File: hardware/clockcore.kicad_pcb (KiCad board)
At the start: 2 copper layers, 75 x 40 mm, 60 parts, among them J1 Header, J2 Ext, J3 JTAG, J7 GCT_USB4108-GF-A, Q1 MBT3904DW1T1G, SW1 Reset, SW2 Boot, U1 AP2114H-3_3TRG1, U2 ‎SN74HCT245PWR‎, U3 ESP32-WROOM-32, U4 DS1338Z-33+, U5 FT231XS, U6 USBLC6-4SC6, Y1 32.768Hz, 12.5pF, 45kΩ

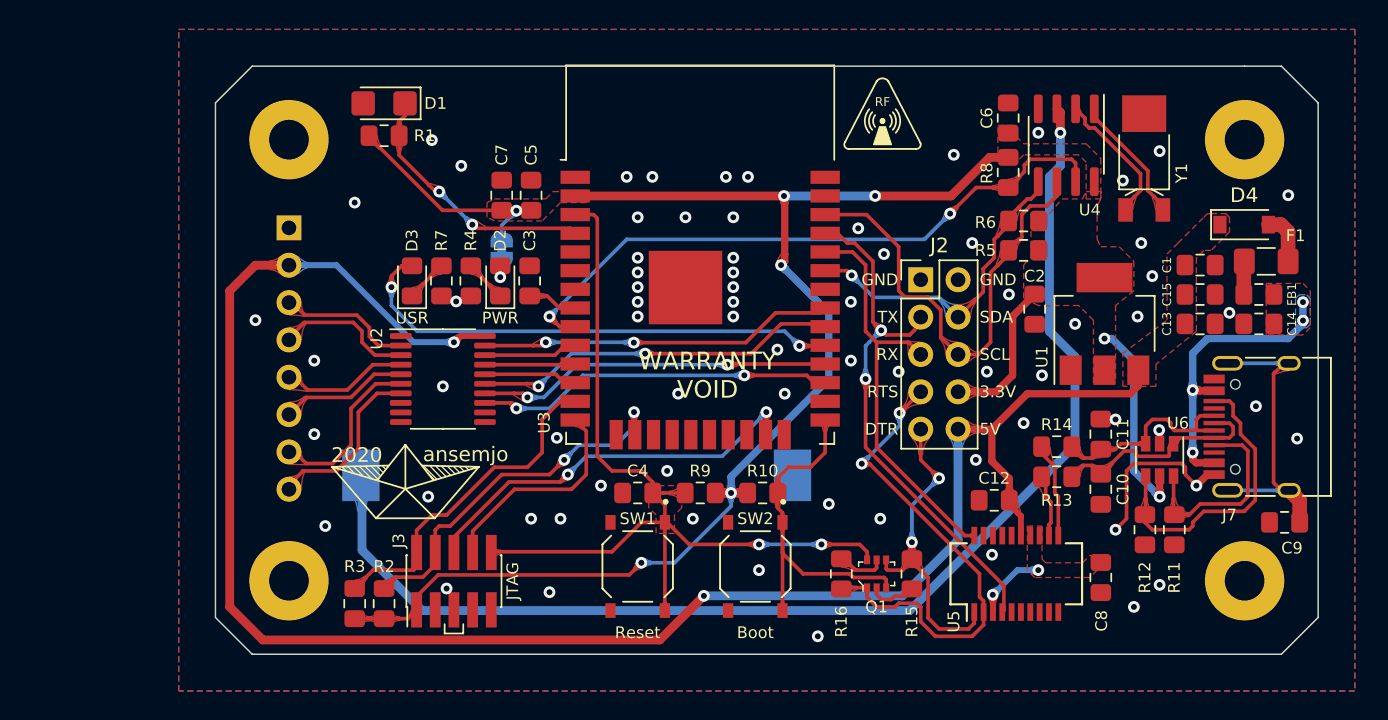
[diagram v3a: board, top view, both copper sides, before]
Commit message: add ds18b20 to clock core and reroute a few traces
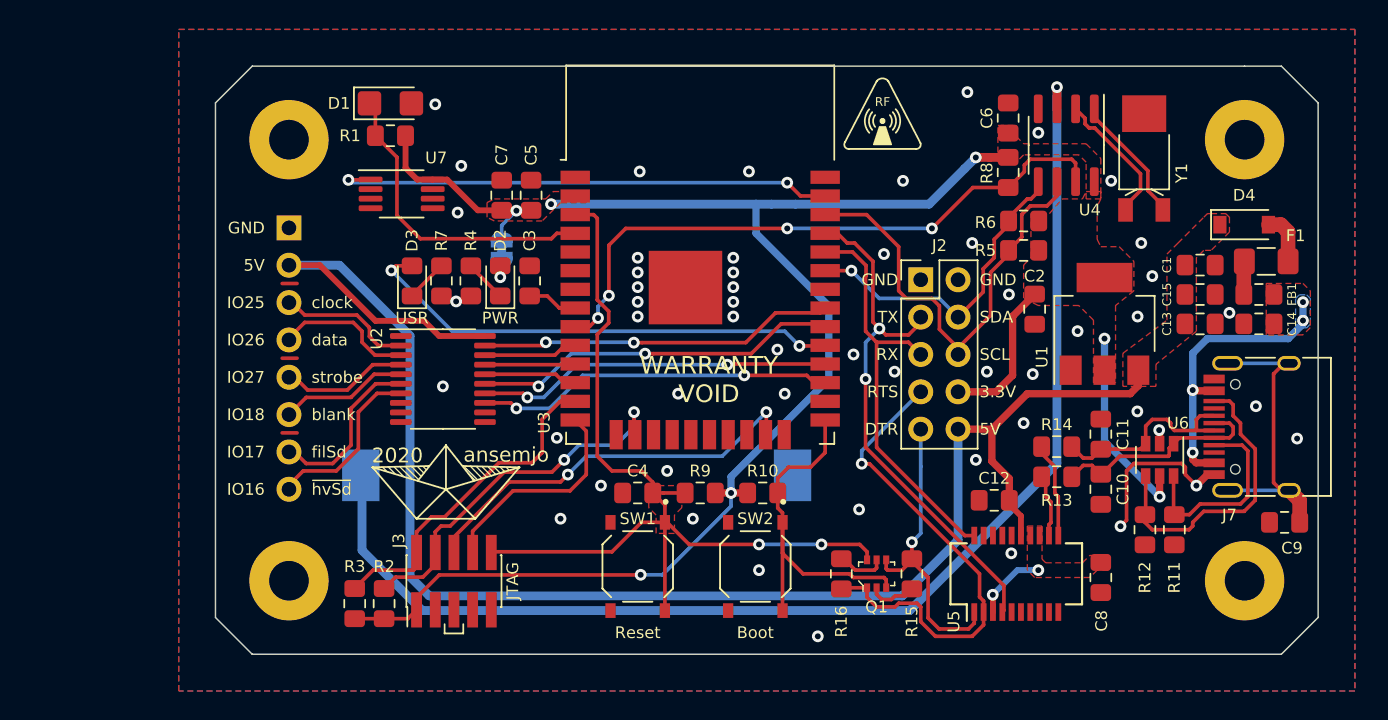
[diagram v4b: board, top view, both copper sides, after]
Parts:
- added U7: DS18B20U, Package_SO:MSOP-8_3x3mm_P0.65mm, F.Cu at (97.7, 56.2)
- moved A1 2.76 mm to (100.7, 76.3)
- moved D1 0.43 mm to (96.9, 50.0), turned to 0 degrees
- moved R1 0.43 mm to (96.9, 52.2), turned to 180 degrees
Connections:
- U3 pad 37: (no net) -> TEMP
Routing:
- net TEMP: track 0.00 -> 34.4 mm, vias 0 -> 2
- net +5V: track 125.4 -> 111.5 mm, vias 2 -> 0
- net LIGHT: track 17.9 -> 21.3 mm, vias 2 -> 0
- net GND: track 12.6 -> 15.3 mm, vias 72 -> 53
- net Net-(BT1-Pad1): track 83.9 -> 85.2 mm
- net IO_LED: track 34.9 -> 33.8 mm
- net SCL: track 31.8 -> 30.7 mm
- net DTR: track 21.8 -> 20.8 mm, vias 2 -> 1
- net RTC_SQW: track 43.9 -> 42.9 mm, vias 2 -> 4
- net CHIP_EN: track 61.3 -> 62.0 mm
- net +3V3: track 126.5 -> 126.8 mm, vias 8 -> 7
- net RTS: vias 2 -> 1
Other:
- board text added: "IO16"
- board text added: "IO17"
- board text added: "IO18"
- board text added: "IO25"
- board text added: "IO26"
- board text added: "IO27"
- board text added: "blank"
- board text added: "clock"
- board text added: "data"
- board text added: "filSd"
- board text added: "strobe"
- board text added: "~hvSd~"

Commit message: updated crystal in schematic so pin3 is gnd, added teardrops
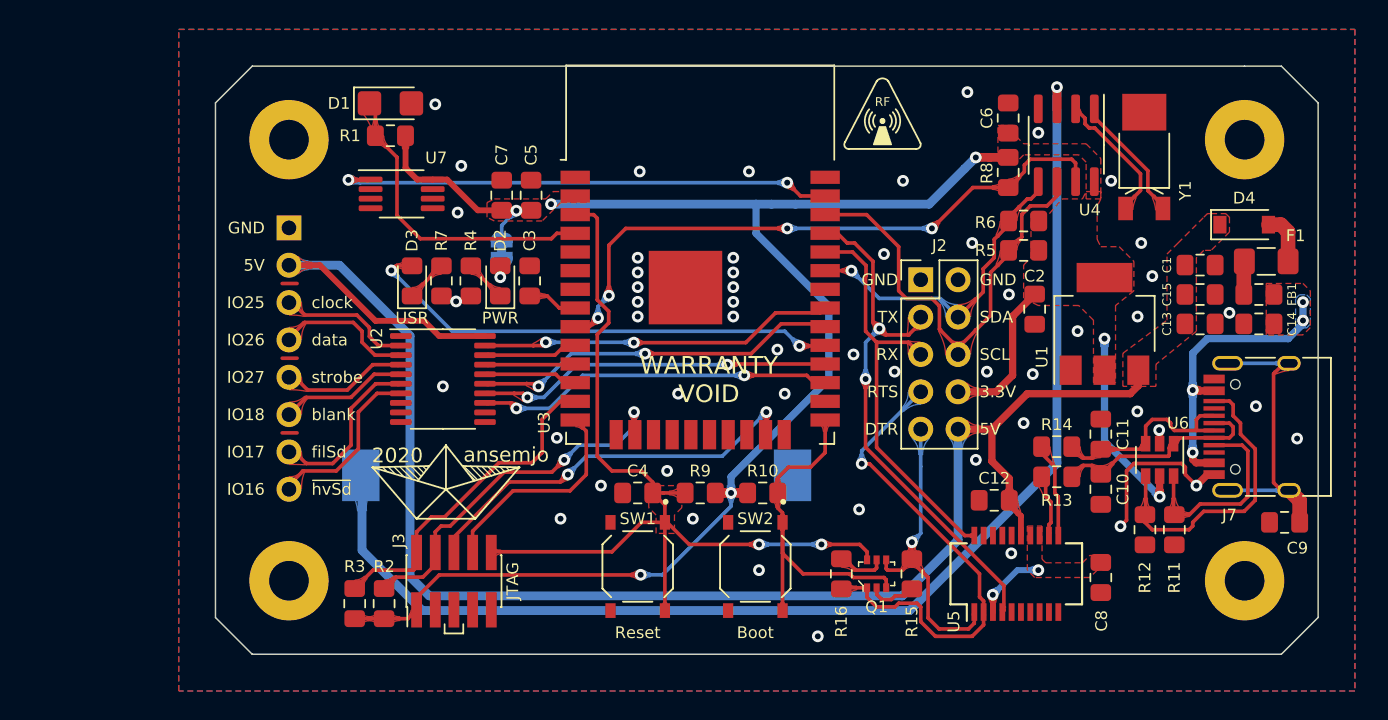
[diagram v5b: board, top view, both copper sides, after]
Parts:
- moved Y1 0.10 mm to (148.2, 53.7)
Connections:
- Y1 pad 3: (no net) -> GND
